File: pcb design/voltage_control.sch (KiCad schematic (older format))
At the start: 10 parts, among them Q19 PNP, U12 OPA2172

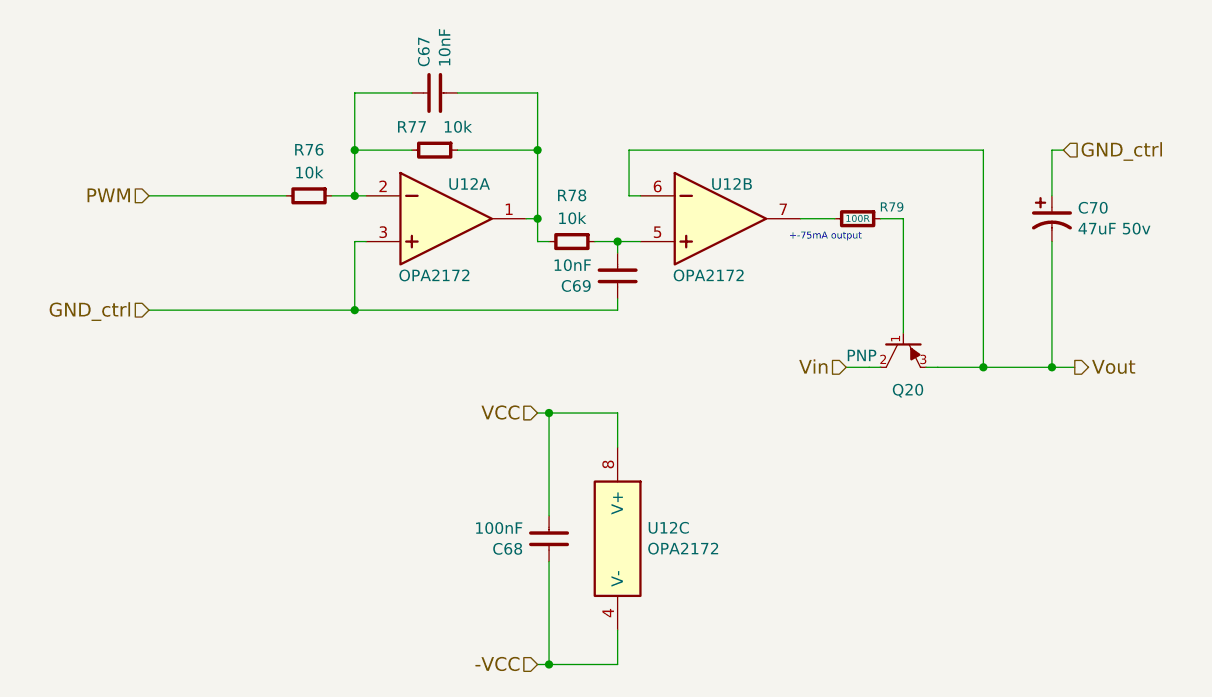
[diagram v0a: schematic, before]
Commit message: Removed old comments, added notes, connected programmable -VEE
Signed-off-by: Marcos Chaparro <mchaparro@paltatech.com>
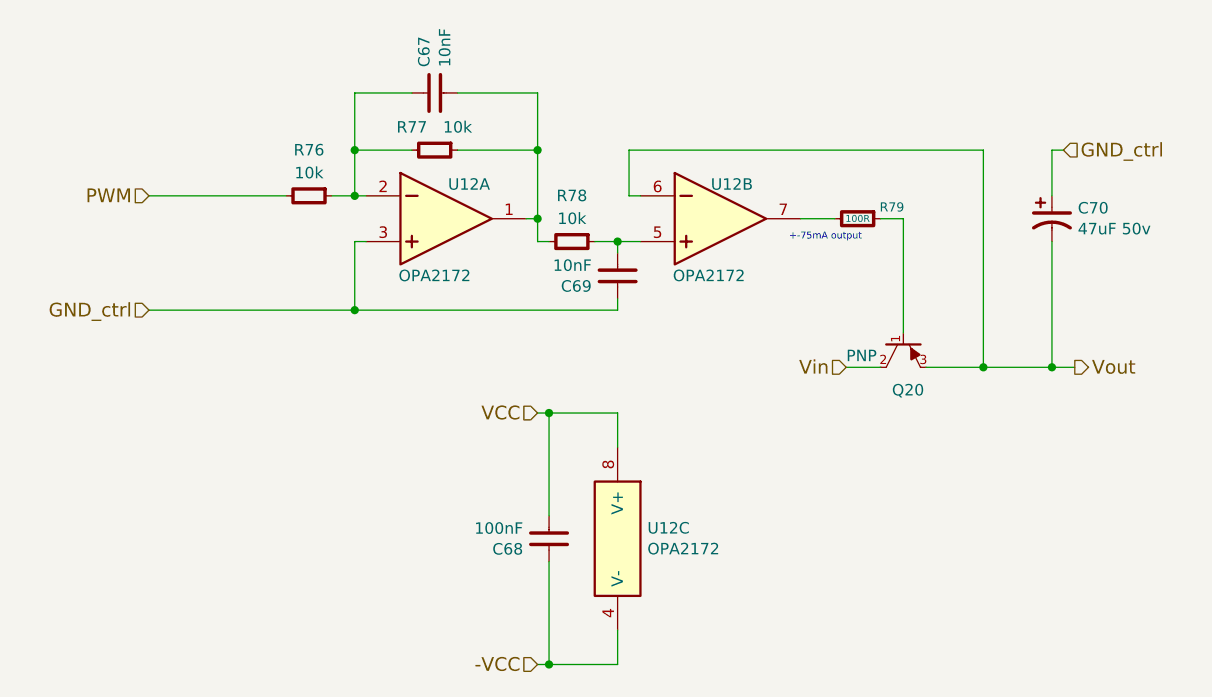
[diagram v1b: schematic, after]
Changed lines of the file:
@@
 	6050 3850 5900 3850
 Wire Wire Line
-	6450 4500 6500 4500
-Wire Wire Line
-	6500 4500 6700 4500
-Wire Wire Line
-	6700 4500 7000 4500
-Wire Wire Line
-	7000 4500 7100 4500
-Wire Wire Line
-	6250 4500 6200 4500
-Wire Wire Line
-	6200 4500 6100 4500
+	6450 4500 7100 4500
+Wire Wire Line
+	6100 4500 6250 4500
 Text HLabel 6100 4500 0    60   Input ~ 0
 Vin
@@
 	4750 3850 4700 3850
 Wire Wire Line
-	4750 3300 4750 3550
-Wire Wire Line
-	4750 3550 4750 3850
-Wire Wire Line
-	4750 3850 4750 3950
+	4750 3300 4750 3950
 Wire Wire Line
 	4750 3550 4400 3550
@@
 	4200 3550 3950 3550
 Wire Wire Line
-	3950 3300 3950 3550
-Wire Wire Line
-	3950 3550 3950 3750
-Wire Wire Line
-	3850 3750 3950 3750
-Wire Wire Line
-	3950 3750 4000 3750
+	3950 3300 3950 3750
+Wire Wire Line
+	3850 3750 4000 3750
 Connection ~ 3950 3750
 Wire Wire Line
-	5000 3950 5100 3950
-Wire Wire Line
-	5100 3950 5200 3950
+	5000 3950 5200 3950
 Connection ~ 4750 3850
 Wire Wire Line
@@
 	5100 4250 5100 4200
 Wire Wire Line
-	3050 4250 3950 4250
-Wire Wire Line
-	3950 4250 5100 4250
+	3050 4250 5100 4250
 Wire Wire Line
 	3950 3950 3950 4250
@@
 -VCC
 Wire Wire Line
-	4750 5800 4800 5800
-Wire Wire Line
-	4800 5800 5100 5800
+	4750 5800 5100 5800
 Wire Wire Line
 	5100 5800 5100 5650
 Wire Wire Line
-	5100 4850 5100 4700
-Wire Wire Line
-	5100 4700 4800 4700
-Wire Wire Line
-	4800 4700 4750 4700
+	5100 4700 5100 4850
+Wire Wire Line
+	4750 4700 5100 4700
 Text HLabel 3050 3750 0    60   Input ~ 0
 PWM

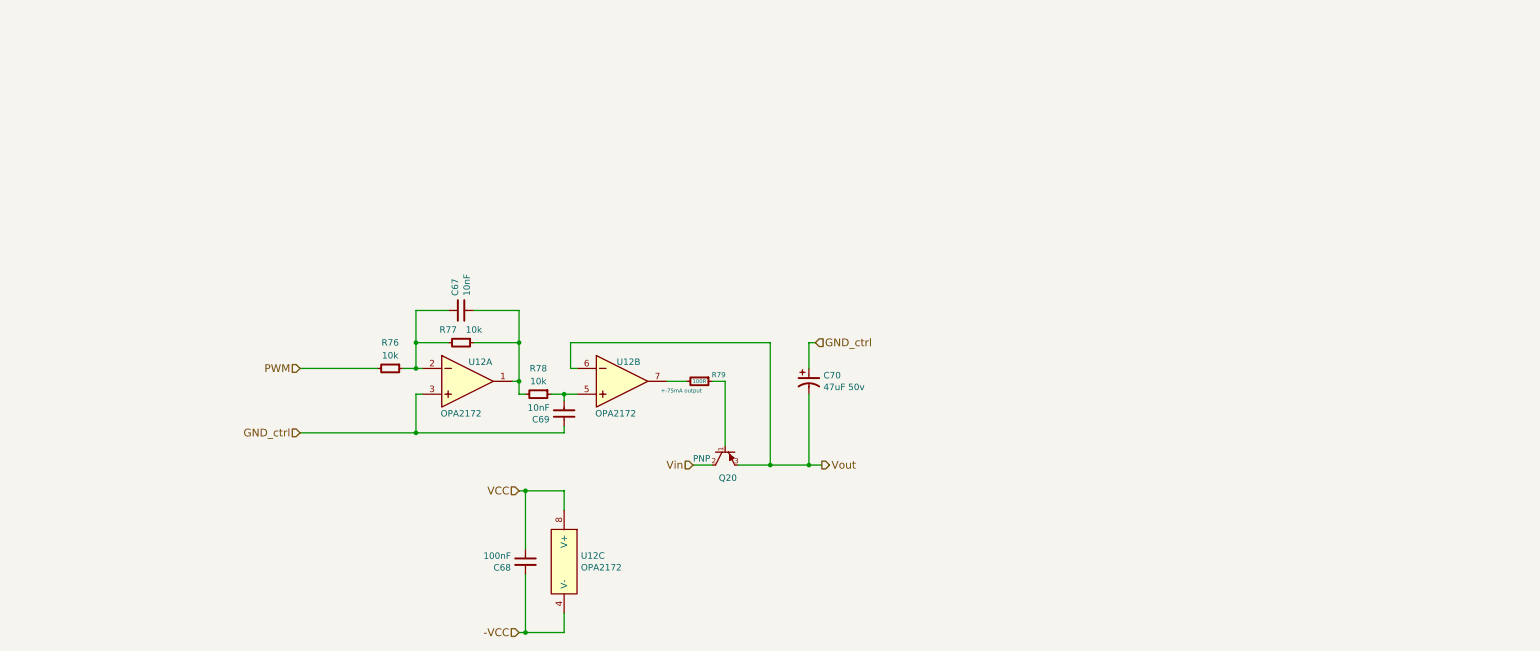
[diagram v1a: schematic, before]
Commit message: Added phase voltage sensing
Signed-off-by: Marcos Chaparro <mchaparro@paltatech.com>
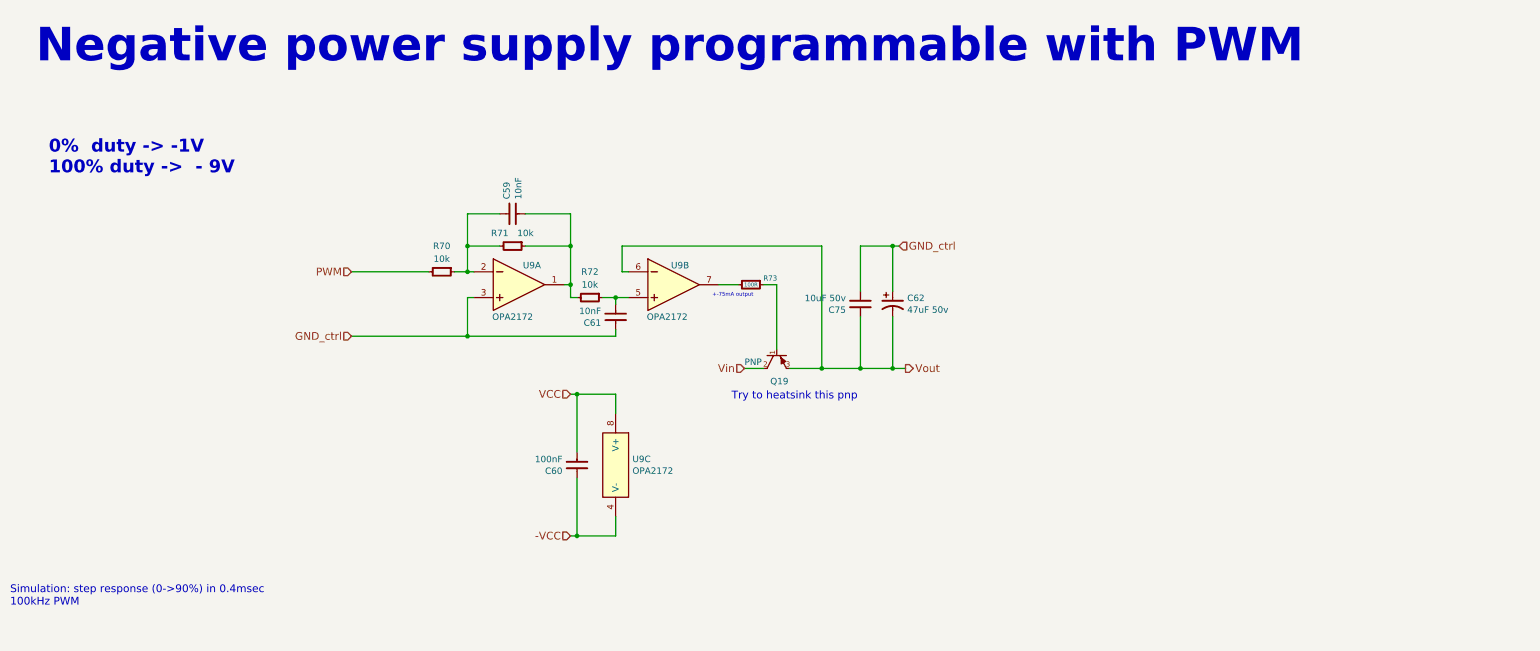
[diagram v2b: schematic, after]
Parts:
- added C75: 10uF 50v, IPC7351-Nominal:CAPC3216X70, symbol C-1206
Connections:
- net GND_ctrl: now also C75.2
- net Vout: now also C75.1
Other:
- note added: "0% duty -> -1V\n100% duty -> - 9V"
- note added: "Negative power supply programmable with PWM"
- note added: "Simulation: step response (0->90%) in 0.4msec\n100kHz PWM\n"
- note added: "Try to heatsink this pnp"
- moved on the sheet: C59, C60, C61, C62, Q19, R70, R71, R72, R73, U9A, U9B, U9C

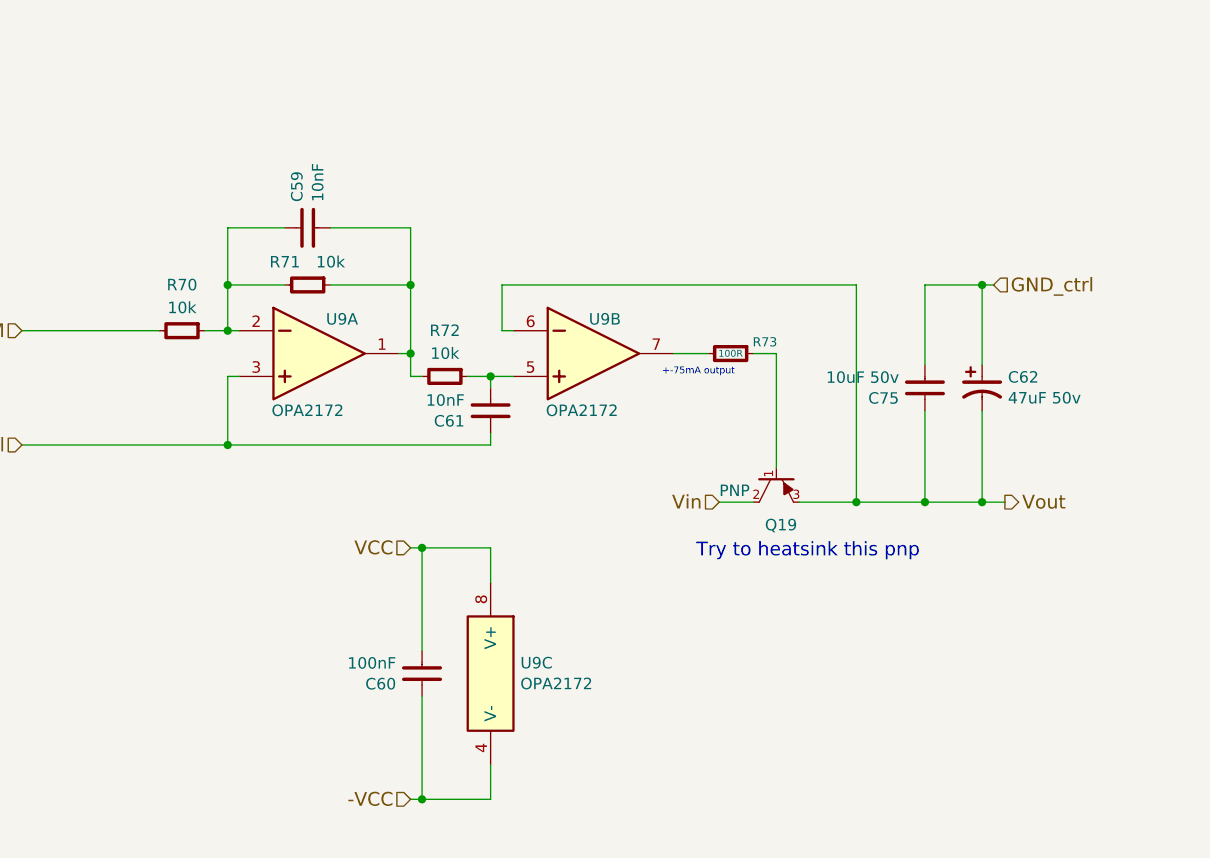
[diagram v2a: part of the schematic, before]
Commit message: Phase voltage sensing laid out
Signed-off-by: Marcos Chaparro <mchaparro@paltatech.com>
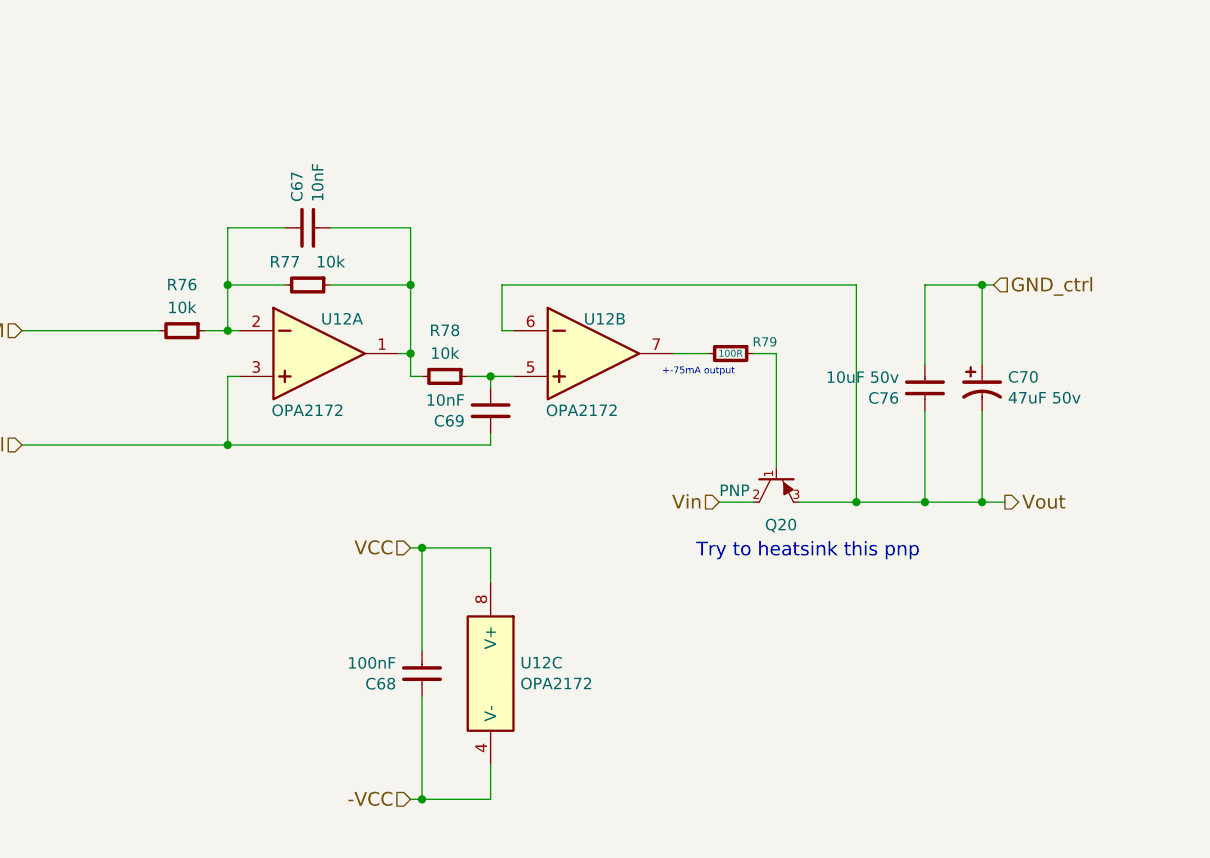
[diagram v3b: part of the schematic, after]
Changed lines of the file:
@@
 AR Path="/5822D62D/5856AA02/5856B1FC" Ref="Q19"  Part="1"
 AR Path="/5824556D/5856AA02/5856B1FC" Ref="Q20"  Part="1"
-F 0 "Q19" V 6900 3650 50  0000 L CNN
+F 0 "Q20" V 6900 3650 50  0000 L CNN
 F 1 "PNP" V 6750 3450 50  0000 L CNN
 F 2 "SMD_Packages:DPAK-2" H 6750 3700 60  0001 C CNN
@@
 AR Path="/5824556D/5856AA02/5856B214" Ref="R76"  Part="1"
 AR Path="/5822D62D/5856AA02/5856B214" Ref="R70"  Part="1"
-F 0 "R70" V 3950 3000 50  0000 C CNN
+F 0 "R76" V 3950 3000 50  0000 C CNN
 F 1 "10k" V 4050 3000 50  0000 C CNN
 F 2 "IPC7351-Nominal:RESC1608X50" H 4150 3000 50  0001 C CNN
@@
 AR Path="/5824556D/5856AA02/5856B21C" Ref="R77"  Part="1"
 AR Path="/5822D62D/5856AA02/5856B21C" Ref="R71"  Part="1"
-F 0 "R71" V 4600 2700 50  0000 C CNN
+F 0 "R77" V 4600 2700 50  0000 C CNN
 F 1 "10k" V 4600 2900 50  0000 C CNN
 F 2 "IPC7351-Nominal:RESC1608X50" H 4700 2800 50  0001 C CNN
@@
 AR Path="/5824556D/5856AA02/5856B237" Ref="C70"  Part="1"
 AR Path="/5822D62D/5856AA02/5856B237" Ref="C62"  Part="1"
-F 0 "C62" H 7763 3296 50  0000 L CNN
+F 0 "C70" H 7763 3296 50  0000 L CNN
 F 1 "47uF 50v" H 7763 3205 50  0000 L CNN
 F 2 "w_smd_cap:c_elec_6.3x7.7" H 7650 3250 50  0001 C CNN
@@
 AR Path="/5824556D/5856AA02/5856B245" Ref="C67"  Part="1"
 AR Path="/5822D62D/5856AA02/5856B245" Ref="C59"  Part="1"
-F 0 "C59" H 4813 2596 50  0000 L CNN
+F 0 "C67" H 4813 2596 50  0000 L CNN
 F 1 "10nF" H 4813 2505 50  0000 L CNN
 F 2 "IPC7351-Nominal:CAPC1608X55" H 4700 2550 50  0001 C CNN
@@
 AR Path="/5824556D/5856AA02/5856B251" Ref="R78"  Part="1"
 AR Path="/5822D62D/5856AA02/5856B251" Ref="R72"  Part="1"
-F 0 "R72" V 5100 3200 50  0000 C CNN
+F 0 "R78" V 5100 3200 50  0000 C CNN
 F 1 "10k" V 5200 3200 50  0000 C CNN
 F 2 "IPC7351-Nominal:RESC1608X50" H 5300 3200 50  0001 C CNN
@@
 AR Path="/5824556D/5856AA02/5856B25A" Ref="C69"  Part="1"
 AR Path="/5822D62D/5856AA02/5856B25A" Ref="C61"  Part="1"
-F 0 "C61" H 5613 3396 50  0000 L CNN
+F 0 "C69" H 5613 3396 50  0000 L CNN
 F 1 "10nF" H 5613 3305 50  0000 L CNN
 F 2 "IPC7351-Nominal:CAPC1608X55" H 5500 3350 50  0001 C CNN
@@
 AR Path="/5824556D/5856AA02/5856B26A" Ref="U12"  Part="1"
 AR Path="/5822D62D/5856AA02/5856B26A" Ref="U9"  Part="1"
-F 0 "U9" H 4850 3250 50  0000 C CNN
+F 0 "U12" H 4850 3250 50  0000 C CNN
 F 1 "OPA2172" H 4700 2850 50  0000 C CNN
 F 2 "IPC7351-Nominal:SOIC127P600X175-8" H 4700 2850 50  0001 C CNN
@@
 AR Path="/5824556D/5856AA02/5856B273" Ref="U12"  Part="2"
 AR Path="/5822D62D/5856AA02/5856B273" Ref="U9"  Part="2"
-F 0 "U9" H 6000 3250 50  0000 C CNN
+F 0 "U12" H 6000 3250 50  0000 C CNN
 F 1 "OPA2172" H 5900 2850 50  0000 C CNN
 F 2 "IPC7351-Nominal:SOIC127P600X175-8" H 5900 2850 50  0001 C CNN
@@
 AR Path="/5824556D/5856AA02/5856B5B6" Ref="U12"  Part="3"
 AR Path="/5822D62D/5856AA02/5856B5B6" Ref="U9"  Part="3"
-F 0 "U9" H 5630 4546 50  0000 L CNN
+F 0 "U12" H 5630 4546 50  0000 L CNN
 F 1 "OPA2172" H 5630 4455 50  0000 L CNN
 F 2 "IPC7351-Nominal:SOIC127P600X175-8" H 5500 4250 50  0001 C CNN
@@
 AR Path="/5824556D/5856AA02/5856B5EA" Ref="C68"  Part="1"
 AR Path="/5822D62D/5856AA02/5856B5EA" Ref="C60"  Part="1"
-F 0 "C60" H 5313 4546 50  0000 L CNN
+F 0 "C68" H 5313 4546 50  0000 L CNN
 F 1 "100nF" H 5313 4455 50  0000 L CNN
 F 2 "IPC7351-Nominal:CAPC1608X55" H 5200 4500 50  0001 C CNN
@@
 AR Path="/5822D62D/5856AA02/58575342" Ref="R73"  Part="1"
 AR Path="/5824556D/5856AA02/58575342" Ref="R79"  Part="1"
-F 0 "R73" V 6500 3250 40  0000 C CNN
+F 0 "R79" V 6500 3250 40  0000 C CNN
 F 1 "100R" V 6550 3100 30  0000 C CNN
 F 2 "IPC7351-Nominal:RESC2012X50" H 6550 3100 50  0001 C CNN
@@
 AR Path="/5822D62D/5856AA02/5858F095" Ref="C75"  Part="1"
 AR Path="/5824556D/5856AA02/5858F095" Ref="C76"  Part="1"
-F 0 "C75" H 7513 3296 50  0000 L CNN
+F 0 "C76" H 7513 3296 50  0000 L CNN
 F 1 "10uF 50v" H 7513 3205 50  0000 L CNN
 F 2 "IPC7351-Nominal:CAPC3216X70" H 7400 3250 50  0001 C CNN
